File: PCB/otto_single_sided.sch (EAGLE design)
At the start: 19 parts, among them M1 ARDUINO-NANO-3.0, M2 SMALL_SERVO, M3 SMALL_SERVO, M4 SMALL_SERVO, M5 SMALL_SERVO

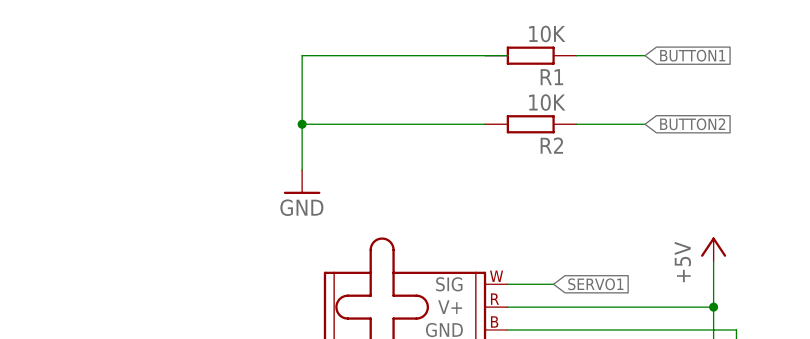
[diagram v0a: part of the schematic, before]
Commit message: connected R1 GND Point
R1 was not connected to GND
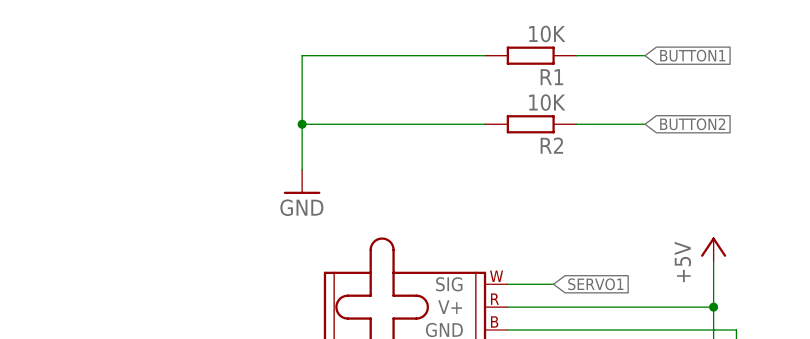
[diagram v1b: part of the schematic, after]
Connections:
- net GND: now also R1.2
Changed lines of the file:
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@@
 <segment>
 <pinref part="GND7" gate="1" pin="GND"/>
-<wire x1="142.24" y1="119.38" x2="119.38" y2="119.38" width="0.1524" layer="91"/>
+<wire x1="139.7" y1="119.38" x2="119.38" y2="119.38" width="0.1524" layer="91"/>
 <wire x1="119.38" y1="119.38" x2="119.38" y2="111.76" width="0.1524" layer="91"/>
 <pinref part="R2" gate="G$1" pin="2"/>
@@
 <wire x1="139.7" y1="111.76" x2="119.38" y2="111.76" width="0.1524" layer="91"/>
 <junction x="119.38" y="111.76"/>
+<pinref part="R1" gate="G$1" pin="2"/>
 </segment>
 <segment>
